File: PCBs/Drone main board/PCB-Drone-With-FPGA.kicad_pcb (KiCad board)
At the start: 4 copper layers, 60 x 100 mm, 216 parts, among them J1001 Conn_02x10, J1002 Conn_02x07, J1003 Conn_02x10, J1004 Conn_02x05, J201 PJ-102A, J601 DX07S016JA1R1500, J801 SMA, J901 Amphenol-1mm-10-header, U1201 10CL040_F484, U301 AP63205WU-7, U401 SC189ZSKTRT, U402 NCP115ASN250T2G, U501 AP63200WU-7, U601 93LCxxBxxOT, U602 FT232H, U603 MT25QL512ABB8ESF-0SIT, U604 W25Q128JVS, U701 ICM-20602, U702 TXB0108PWR, U703 BNO055, U704 DPS422XTSA1, U705 MCP3208, U801 nRF24L01P, U802 RFX2401C, X1401 SiT2001BI-S2-33E-50.000000G, X801 16MHz, Y601 12MHz, Y701 32.7KHz

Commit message: Minor PCB work
Signed-off-by: Eldalote.Electronics <Eldalote.Electronics@gmail.com>
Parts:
- FB601, FB602, FB603: value 600Ohm 2A -> 600Ohm 1.3A; footprint Resistor_SMD:R_0805_2012Metric -> Resistor_SMD:R_0603_1608Metric
- R607, R608, R609: moved to B.Cu
- moved R608 32.6 mm to (127.2, 132.1), turned to 180 degrees
- moved Y601 31.8 mm to (124.0, 127.4), turned to 270 degrees
- moved C612 26.7 mm to (126.2, 127.9), turned to 270 degrees
- moved C608 26.7 mm to (123.8, 125.0)
- moved R609 25.6 mm to (132.2, 132.0)
- moved D601 14.8 mm to (129.6, 130.2)
- moved R607 5.70 mm to (129.1, 124.6), turned to 0 degrees
- moved R604 2.46 mm to (121.0, 127.8), turned to 90 degrees
- moved FB601 0.91 mm to (132.8, 129.1)
- moved C614 0.59 mm to (128.1, 127.2)
- moved C613 0.50 mm to (128.0, 128.3)
- moved FB602 0.19 mm to (125.0, 130.2)
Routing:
- net VBUS: track 9.07 -> 18.1 mm
- net GND: track 271.4 -> 265.8 mm, vias 327 -> 330
- net Net-(C608-Pad1): track 0.42 -> 5.79 mm
- net Net-(C612-Pad1): track 0.00 -> 4.38 mm
- net /USB and Flash Memory/EECLK: track 11.5 -> 8.56 mm
- net Net-(J601-Pad3): track 0.00 -> 2.44 mm, vias 0 -> 1
- net Net-(R607-Pad1): track 4.96 -> 2.59 mm, vias 0 -> 1
- net Net-(J601-Pad9): track 0.00 -> 2.18 mm, vias 0 -> 1
- net User_flash_CSn: track 51.4 -> 52.8 mm
- net /USB and Flash Memory/USB-D+: track 11.2 -> 10.3 mm
- net Net-(D601-Pad5): track 0.00 -> 0.78 mm
- net Net-(C613-Pad1): track 5.40 -> 6.12 mm
- net +3V3: track 165.6 -> 165.1 mm

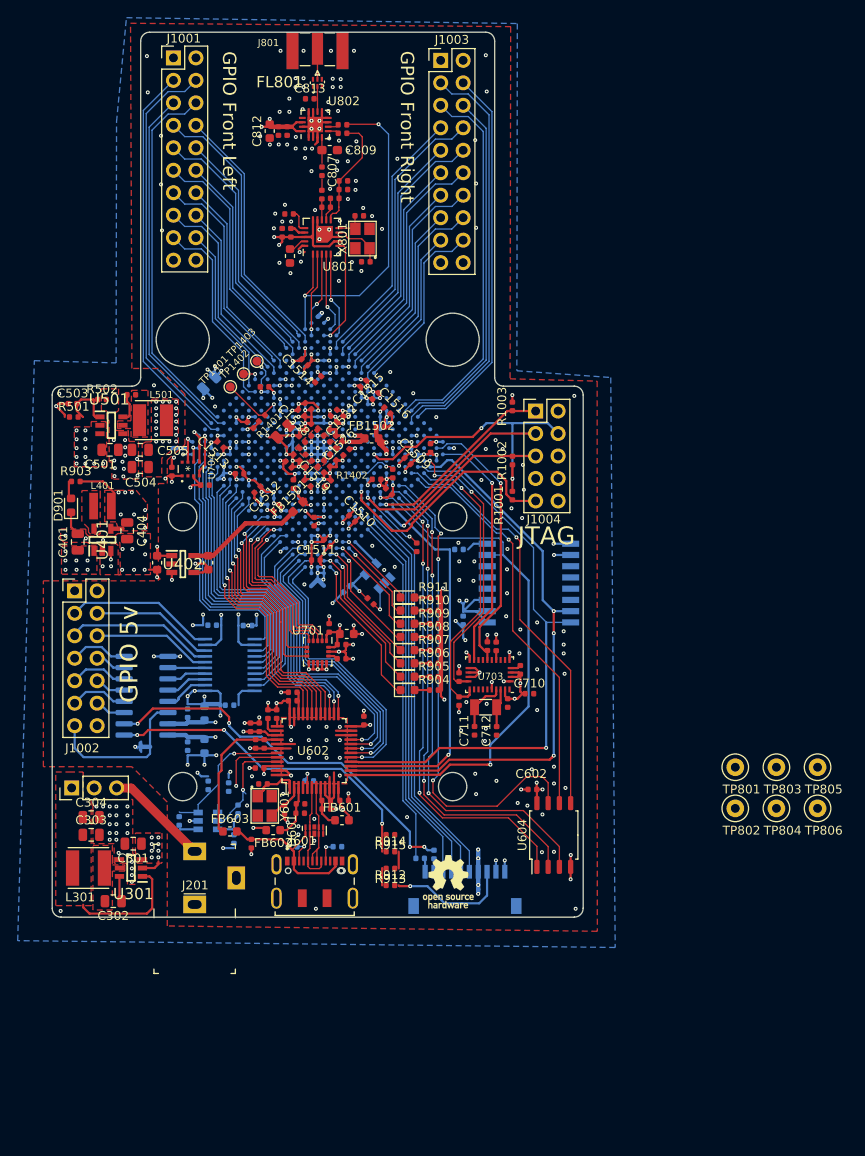
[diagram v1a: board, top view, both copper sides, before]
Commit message: Finished redoing PCB.
Signed-off-by: Eldalote.Electronics <Eldalote.Electronics@gmail.com>
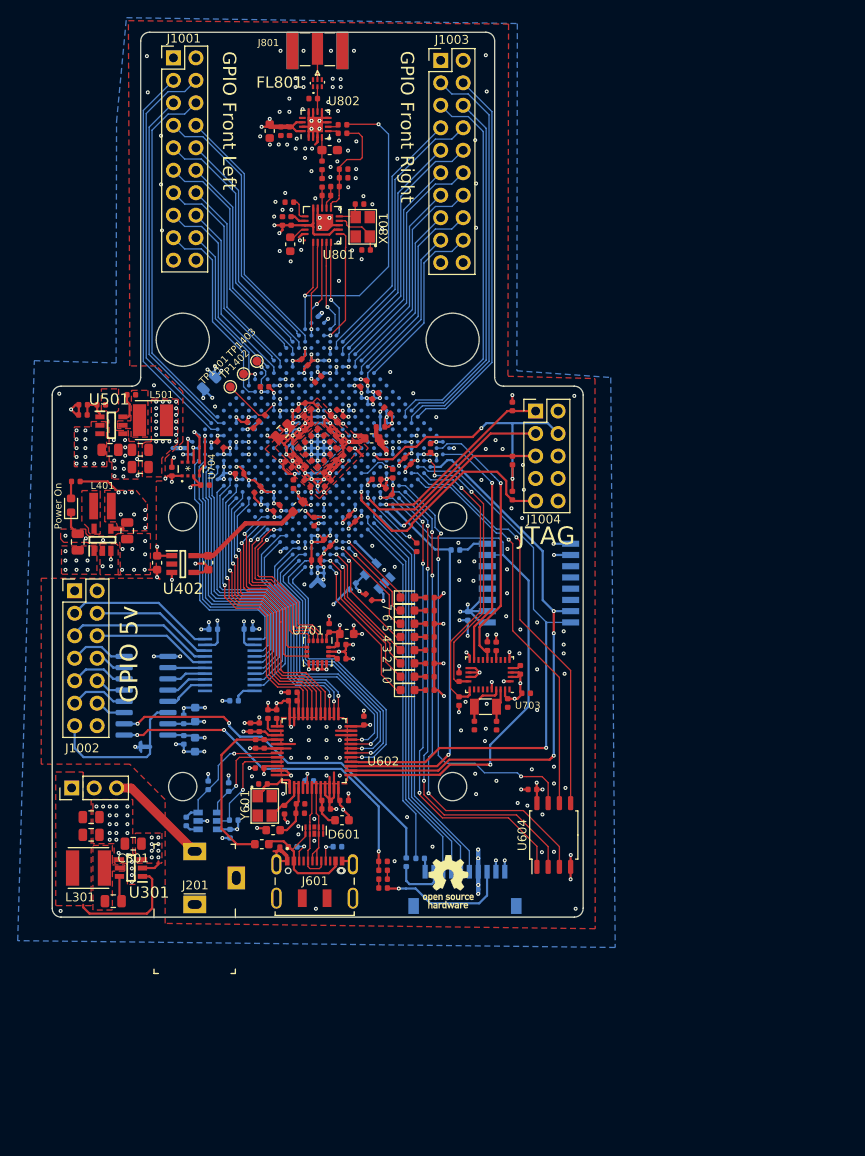
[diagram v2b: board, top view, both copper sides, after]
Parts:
- removed TP801, TP802, TP803, TP804, TP805, TP806: TestPoint, TestPoint:TestPoint_Loop_D2.50mm_Drill1.0mm
- moved FB603 3.89 mm to (123.7, 131.8)
- moved C620 3.73 mm to (126.2, 132.1), turned to 180 degrees
- moved R901 3.25 mm to (140.0, 133.8)
- moved R915 3.13 mm to (137.4, 133.7)
- moved R914 2.27 mm to (137.4, 134.7)
- moved R913 1.47 mm to (137.4, 135.7)
- moved C801 1.33 mm to (126.9, 64.0)
- moved L802 1.33 mm to (132.0, 57.4)
- moved C802 1.33 mm to (127.0, 61.3)
- moved C803 1.33 mm to (126.0, 61.3)
- moved C804 1.33 mm to (135.5, 64.6)
- moved C805 1.33 mm to (134.7, 59.4)
- moved C806 1.33 mm to (132.9, 55.5)
- moved C808 1.33 mm to (132.9, 56.5)
- moved L801 1.33 mm to (131.0, 58.5)
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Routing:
- net +1V2: track 84.7 -> 123.9 mm
- net User_flash_IO3: track 55.1 -> 49.0 mm
- net +5V: track 21.1 -> 15.3 mm
- net Net-(J901-Pad9): track 1.46 -> 6.16 mm
- net /USB and Flash Memory/5v-USB: track 15.9 -> 19.9 mm
- net VBUS: track 18.1 -> 14.5 mm
- net GND: track 265.8 -> 269.3 mm, vias 330 -> 329
- net /USB and Flash Memory/EECLK: track 8.56 -> 11.7 mm
- net ADC_CH1: track 44.0 -> 41.0 mm, vias 4 -> 2
- net +3V3: track 165.1 -> 162.2 mm, vias 73 -> 75
- net /Power Distribution and Estimation/1v2 power regulator/1v2_FB: track 6.45 -> 3.76 mm
- net ADC_CH0: track 37.8 -> 39.9 mm
- net nRF_MOSI: track 9.12 -> 10.5 mm
- net nRF_MISO: track 9.80 -> 11.1 mm
- net nRF_CSn: track 9.48 -> 10.8 mm
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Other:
- board text added: "7 6 5 4 3 2 1 0"
- board text added: "Power On"
